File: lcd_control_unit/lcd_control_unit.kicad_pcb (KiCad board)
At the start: 2 copper layers, 1 part

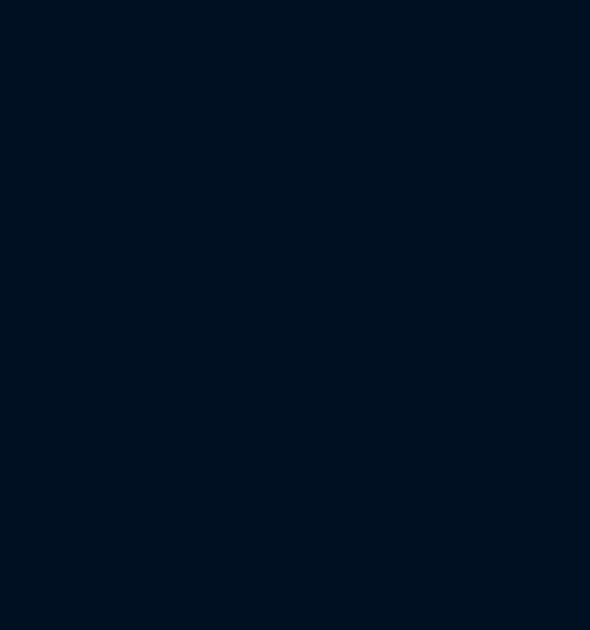
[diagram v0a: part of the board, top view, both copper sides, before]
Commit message: fix: back light circuitry and data lines
A resistor was missing for the base of the transistor. The data lines
were also not wired correctly

Signed-off-by: Scott Gibb <smgibb@yahoo.com>
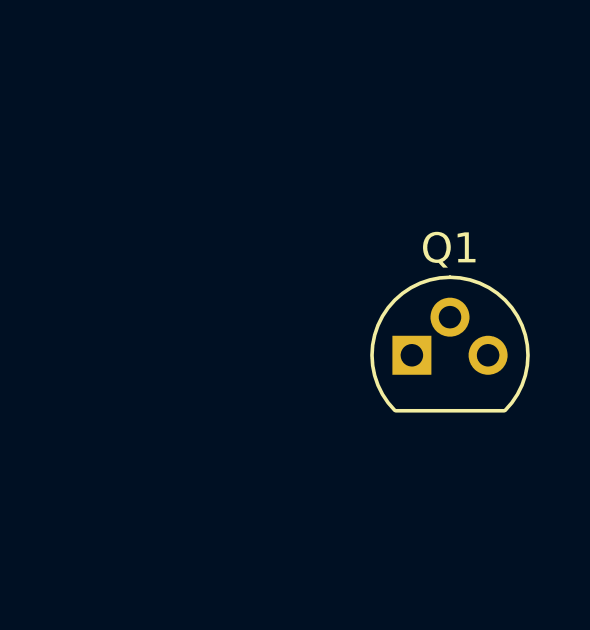
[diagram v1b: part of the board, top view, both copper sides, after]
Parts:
- added Q1: 2N2222, Package_TO_SOT_THT:TO-92, F.Cu at (153.0, 58.8)
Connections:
- DS1 pad 1: unconnected-(DS1-VSS-Pad1) -> GND
- DS1 pad 10: unconnected-(DS1-D3-Pad10) -> Net-(DS1-D3)
- DS1 pad 15: unconnected-(DS1-LED(+)-Pad15) -> +5V
- DS1 pad 16: unconnected-(DS1-LED(-)-Pad16) -> Net-(DS1-LED(-))
- DS1 pad 2: unconnected-(DS1-VDD-Pad2) -> +5V
- DS1 pad 3: unconnected-(DS1-VO-Pad3) -> Net-(DS1-VO)
- DS1 pad 4: unconnected-(DS1-RS-Pad4) -> Net-(DS1-RS)
- DS1 pad 5: unconnected-(DS1-R/W-Pad5) -> Net-(DS1-R/W)
- DS1 pad 6: unconnected-(DS1-E-Pad6) -> Net-(DS1-E)
- DS1 pad 7: unconnected-(DS1-D0-Pad7) -> Net-(DS1-D0)
- DS1 pad 8: unconnected-(DS1-D1-Pad8) -> Net-(DS1-D1)
- DS1 pad 9: unconnected-(DS1-D2-Pad9) -> Net-(DS1-D2)
